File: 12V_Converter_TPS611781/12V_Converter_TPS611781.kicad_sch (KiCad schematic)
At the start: 20 parts, among them M1 CSD17308Q3T, U1 LM51561DSSR

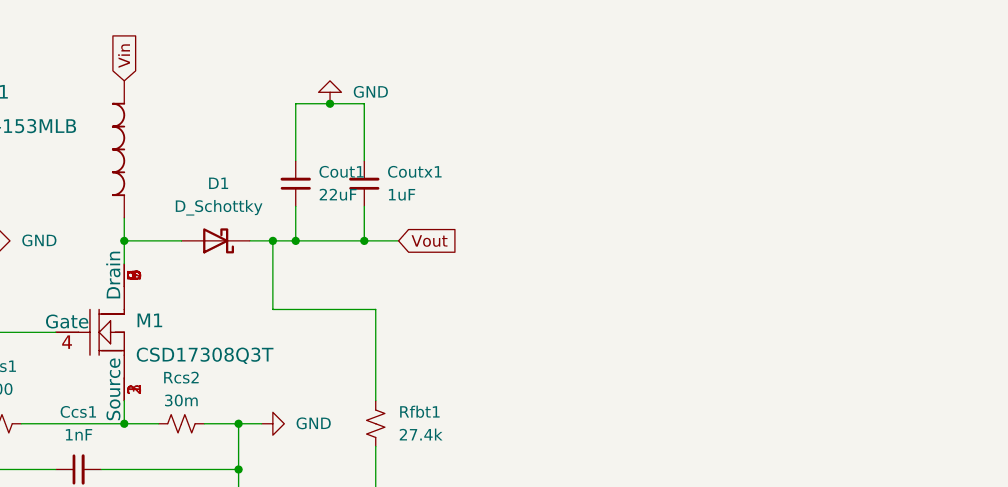
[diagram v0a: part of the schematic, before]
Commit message: notes on diodes
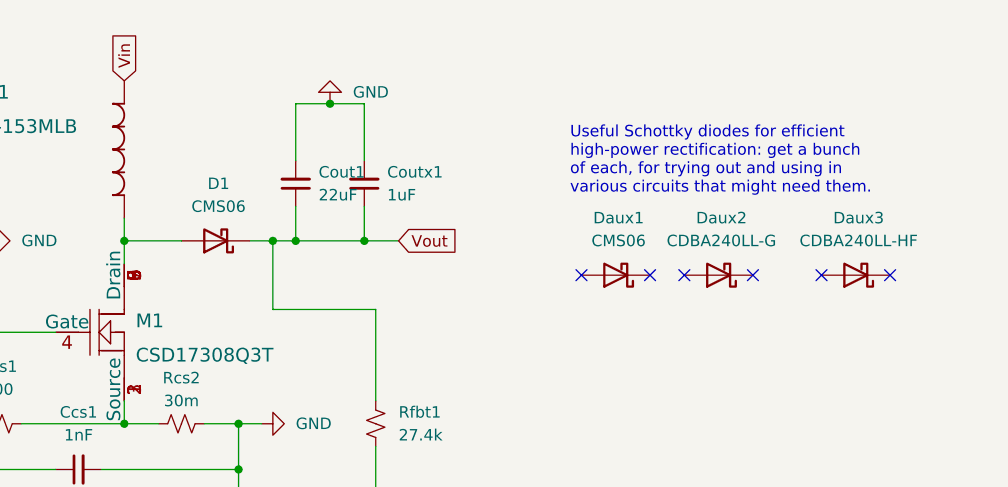
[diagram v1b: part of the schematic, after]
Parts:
- added Daux1: CMS06, symbol Device:D_Schottky
- added Daux2: CDBA240LL-G, symbol Device:D_Schottky
- added Daux3: CDBA240LL-HF, symbol Device:D_Schottky
- D1: value D_Schottky -> CMS06
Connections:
- no-connect marks 1 -> 7
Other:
- note added: "Useful Schottky diodes for efficient high-power rectification: get a bunch of each, for trying out and using in various circuits that might need them."
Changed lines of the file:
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@@
   (junction (at 179.07 97.79) (diameter 0) (color 0 0 0 0)
   )
+  (no_connect (at 229.87 81.28))
+  (no_connect (at 237.49 81.28))
   (no_connect (at 107.95 100.33))
+  (no_connect (at 256.54 81.28))
+  (no_connect (at 248.92 81.28))
+  (no_connect (at 241.3 81.28))
+  (no_connect (at 264.16 81.28))
   (wire (pts (xy 99.06 123.19) (xy 93.98 123.19))
     (stroke (width 0) (type default) (color 0 0 0 0))
@@
   (wire (pts (xy 179.07 77.47) (xy 179.07 80.01))
     (stroke (width 0) (type default) (color 0 0 0 0))
+  )
+  (text "Useful Schottky diodes for efficient\nhigh-power rectification: get a bunch\nof each, for trying out and using in\nvarious circuits that might need them."
+    (at 228.6 72.39 0)
+    (effects (font (size 1.27 1.27)) (justify left bottom))
   )
   (global_label "Vin" (shape input) (at 179.07 59.69 90) (fields_autoplaced)
@@
     (pin "2")
   )
+  (symbol (lib_id "Device:D_Schottky") (at 233.68 81.28 180) (unit 1)
+    (in_bom yes) (on_board no) (fields_autoplaced)
+    (property "Reference" "Daux1" (id 0) (at 233.9975 74.93 0))
+    (property "Value" "CMS06" (id 1) (at 233.9975 77.47 0))
+    (property "Footprint" "" (id 2) (at 233.68 81.28 0)
+      (effects (font (size 1.27 1.27)) hide)
+    )
+    (property "Datasheet" "~" (id 3) (at 233.68 81.28 0)
+      (effects (font (size 1.27 1.27)) hide)
+    )
+    (pin "1")
+    (pin "2")
+  )
   (symbol (lib_id "Device:C_Small") (at 205.74 71.12 180) (unit 1)
     (in_bom yes) (on_board yes) (fields_autoplaced)
@@
     (pin "2")
   )
+  (symbol (lib_id "Device:D_Schottky") (at 260.35 81.28 180) (unit 1)
+    (in_bom yes) (on_board no) (fields_autoplaced)
+    (property "Reference" "Daux3" (id 0) (at 260.6675 74.93 0))
+    (property "Value" "CDBA240LL-HF" (id 1) (at 260.6675 77.47 0))
+    (property "Footprint" "" (id 2) (at 260.35 81.28 0)
+      (effects (font (size 1.27 1.27)) hide)
+    )
+    (property "Datasheet" "~" (id 3) (at 260.35 81.28 0)
+      (effects (font (size 1.27 1.27)) hide)
+    )
+    (pin "1")
+    (pin "2")
+  )
   (symbol (lib_id "Device:R_Small_US") (at 101.6 107.95 90) (unit 1)
     (in_bom yes) (on_board yes)
@@
     )
     (property "Datasheet" "~" (id 3) (at 101.6 107.95 0)
+      (effects (font (size 1.27 1.27)) hide)
+    )
+    (pin "1")
+    (pin "2")
+  )
+  (symbol (lib_id "Device:D_Schottky") (at 245.11 81.28 180) (unit 1)
+    (in_bom yes) (on_board no) (fields_autoplaced)
+    (property "Reference" "Daux2" (id 0) (at 245.4275 74.93 0))
+    (property "Value" "CDBA240LL-G" (id 1) (at 245.4275 77.47 0))
+    (property "Footprint" "" (id 2) (at 245.11 81.28 0)
+      (effects (font (size 1.27 1.27)) hide)
+    )
+    (property "Datasheet" "~" (id 3) (at 245.11 81.28 0)
       (effects (font (size 1.27 1.27)) hide)
     )
@@
     (in_bom yes) (on_board yes) (fields_autoplaced)
     (property "Reference" "D1" (id 0) (at 189.5475 71.12 0))
-    (property "Value" "D_Schottky" (id 1) (at 189.5475 73.66 0))
+    (property "Value" "CMS06" (id 1) (at 189.5475 73.66 0))
     (property "Footprint" "Diode_SMD:D_SOD-128" (id 2) (at 189.23 77.47 0)
       (effects (font (size 1.27 1.27)) hide)
@@
     )
     (path "/f0bdfea9-aa78-4c8d-9d8f-d4a0a0c87be1"
-      (reference "D1") (unit 1) (value "D_Schottky") (footprint "Diode_SMD:D_SOD-128")
+      (reference "D1") (unit 1) (value "CMS06") (footprint "Diode_SMD:D_SOD-128")
+    )
+    (path "/9779ce16-3c39-4fea-b79d-9c628c9fd4f0"
+      (reference "Daux1") (unit 1) (value "CMS06") (footprint "")
+    )
+    (path "/b8d64ab2-1148-4fd0-be52-89ce33214e76"
+      (reference "Daux2") (unit 1) (value "CDBA240LL-G") (footprint "")
+    )
+    (path "/b14663c6-3479-459d-b6fd-32a79b733e7a"
+      (reference "Daux3") (unit 1) (value "CDBA240LL-HF") (footprint "")
     )
     (path "/9696d93e-8c32-47f6-a582-baf72ef636fe"
